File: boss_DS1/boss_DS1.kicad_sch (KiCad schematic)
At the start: 83 parts, among them J2 Jack_6.35, J3 Conn_01x05, J4 Conn_01x05, J5 Conn_01x05, J6 Jack_6.35, J7 Conn_01x01_Socket, J8 Conn_01x01_Socket, J9 Barrel_Jack_Switch, P1 boss_DS1_front_panel, Q1 MMBT5551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

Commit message: Updated front.
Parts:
- added P2: bottom_panel, pedale:bottom_plate, symbol pedale:boss_DS1_front_panel
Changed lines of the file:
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@@
+	)
+	(symbol
+		(lib_id "pedale:boss_DS1_front_panel")
+		(at 242.57 161.29 0)
+		(unit 1)
+		(exclude_from_sim yes)
+		(in_bom no)
+		(on_board yes)
+		(dnp yes)
+		(fields_autoplaced yes)
+		(property "Reference" "P2"
+			(at 245.11 160.0199 0)
+			(effects
+				(font
+					(size 1.27 1.27)
+				)
+				(justify left)
+			)
+		)
+		(property "Value" "bottom_panel"
+			(at 245.11 162.5599 0)
+			(effects
+				(font
+					(size 1.27 1.27)
+				)
+				(justify left)
+			)
+		)
+		(property "Footprint" "pedale:bottom_plate"
+			(at 242.57 161.29 0)
+			(effects
+				(font
+					(size 1.27 1.27)
+				)
+				(hide yes)
+			)
+		)
+		(property "Datasheet" "~"
+			(at 242.57 161.29 0)
+			(effects
+				(font
+					(size 1.27 1.27)
+				)
+				(hide yes)
+			)
+		)
+		(property "Description" "Potentiometer"
+			(at 242.57 161.29 0)
+			(effects
+				(font
+					(size 1.27 1.27)
+				)
+				(hide yes)
+			)
+		)
+		(instances
+			(project "boss_DS1"
+				(path "/e0801131-6974-42d8-8070-4ed960891aa7"
+					(reference "P2")
+					(unit 1)
+				)
+			)
+		)
 	)
 	(symbol

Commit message: Updated libs.
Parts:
- SW1: footprint pedale:foot_switch_tht_and_floating -> pedale:foot_switch_tht_no_pad
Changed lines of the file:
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@@
 			)
 		)
-		(property "Footprint" "pedale:foot_switch_tht_and_floating"
+		(property "Footprint" "pedale:foot_switch_tht_no_pad"
 			(at 168.91 106.68 0)
 			(effects
@@
 			)
 		)
-		(property "Footprint" "pedale:foot_switch_tht_and_floating"
+		(property "Footprint" "pedale:foot_switch_tht_no_pad"
 			(at 168.91 121.92 0)
 			(effects

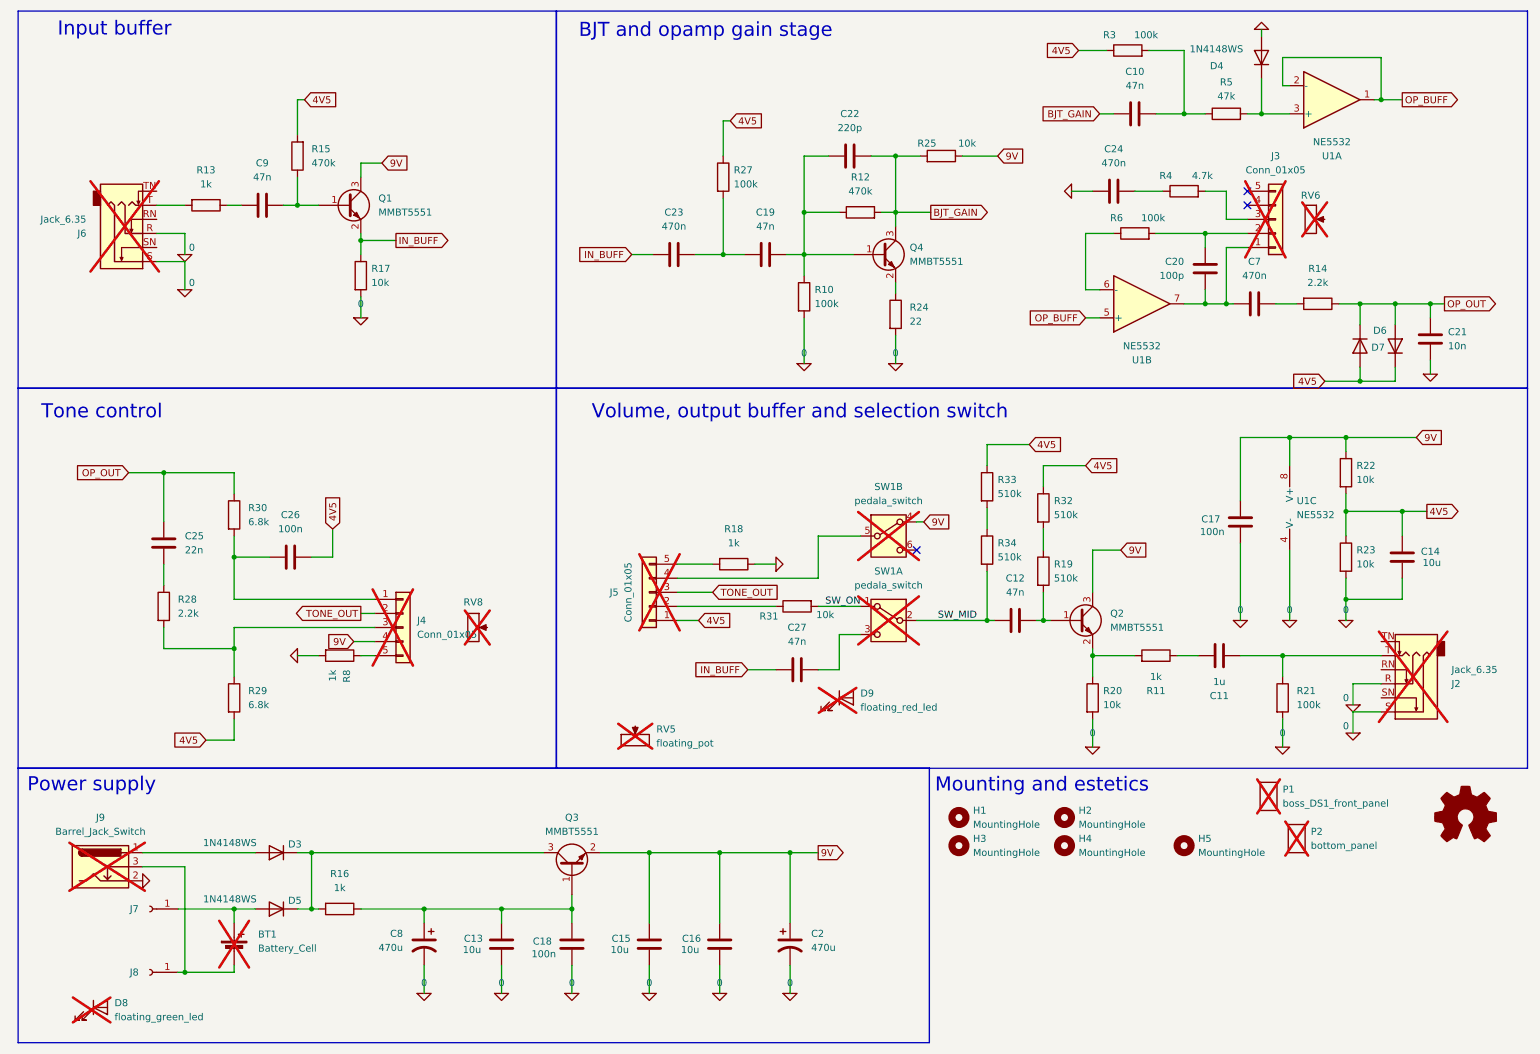
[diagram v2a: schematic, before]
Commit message: Potentiometers checked.
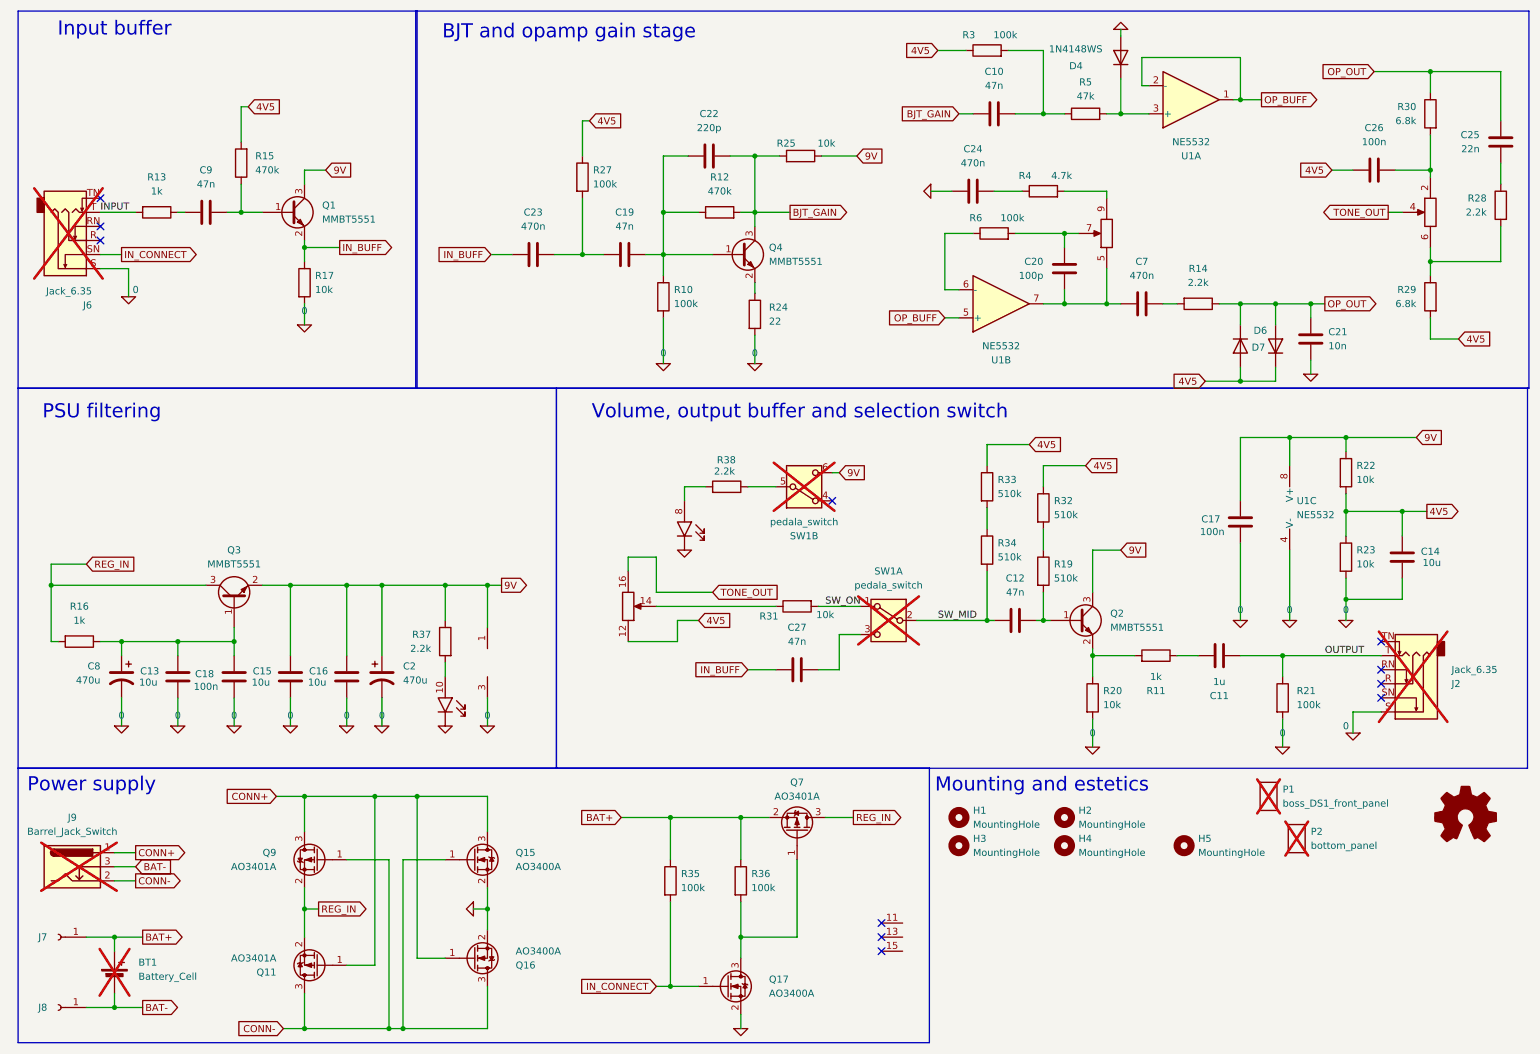
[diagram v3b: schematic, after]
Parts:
- removed D3, D5: 1N4148WS, Diode_SMD:D_SOD-323, symbol Diode:1N4148WS
- removed D8: floating_green_led, pedale:floating_green_led, symbol pedale:floating_green_led
- removed D9: floating_red_led, pedale:floating_red_led, symbol pedale:floating_red_led
- removed J3, J4, J5: Conn_01x05, Connector_JST:JST_EH_B5B-EH-A_1x05_P2.50mm_Vertical, symbol Connector_Generic:Conn_01x05
- removed R18, R8: 1k, Resistor_SMD:R_0603_1608Metric_Pad0.98x0.95mm_HandSolder, symbol Device:R
- removed RV5, RV6, RV8: floating_pot, pedale:floating_pot, symbol pedale:floating_pot
- added J1: top_panel_connector, Connector_IDC:IDC-Header_2x08_P2.54mm_Vertical, symbol pedale:top_panel_connector
- added Q11, Q7, Q9: AO3401A, Package_TO_SOT_SMD:SOT-23, symbol Transistor_FET:AO3401A
- added Q15, Q16, Q17: AO3400A, Package_TO_SOT_SMD:SOT-23, symbol Transistor_FET:AO3400A
- added R35, R36: 100k, Resistor_SMD:R_0603_1608Metric_Pad0.98x0.95mm_HandSolder, symbol Device:R
- added R37, R38: 2.2k, Resistor_SMD:R_0603_1608Metric_Pad0.98x0.95mm_HandSolder, symbol Device:R
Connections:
- net 0: now also J1.3 (GND), Q15.2 (S), Q16.2 (S), Q17.2 (S); no longer J2.R, J6.R, J9.2
- net 4V5: now also J1.12 (Pin_12)
- net 9V: now also SW1.6 (C), J1.1 (VCC), R37.1; no longer SW1.4 (A)
- net TONE_OUT: now also J1.16 (Pin_16), J1.4 (Pin_4)
- net REG_IN: now reaches Q3.3 (C), R16.2
- net REG_IN: now also Q11.2 (S), Q7.3 (D), Q9.2 (S)
- net at C26.1, R30.2: now also J1.2 (Pin_2)
- net at R28.2, R29.1: now also J1.6 (Pin_6)
- net BAT+: now reaches BT1.1 (+), J7.1 (Pin_1)
- net BAT+: now also Q7.2 (S), R35.1, R36.1
- net CONN+: now reaches J9.1
- net CONN+: now also Q11.1 (G), Q15.3 (D), Q16.1 (G), Q9.3 (D)
- net BAT-: now reaches BT1.2 (-), J8.1 (Pin_1), J9.3
- net at SW1.5 (B): now also R38.1
- net OUTPUT: now reaches C11.2, J2.T, R21.1
- net at R31.1: now also J1.14 (Pin_14)
- net at R4.2: now also J1.9 (Pin_9)
- net at C20.1, C7.1, U1.7: now also J1.5 (Pin_5)
- net at C20.2, R6.2: now also J1.7 (Pin_7)
- net IN_CONNECT: now reaches J6.SN
- net IN_CONNECT: now also Q17.1 (G), R35.2
- net INPUT: now reaches J6.T, R13.2
- new net: J1.10 (Pin_10), R37.2
- new net: Q17.3 (D), Q7.1 (G), R36.2
- new net: J1.8 (Pin_8), R38.2
- new net CONN-: J9.2, Q11.3 (D), Q15.1 (G), Q16.3 (D), Q9.1 (G)
- no-connect marks 3 -> 11
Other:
- note added: "PSU filtering"
- note removed: "Tone control"
- moved on the sheet: BT1, C10, C13, C15, C16, C18, C19, C2, C20, C21, C22, C23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

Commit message: Pots again, done.
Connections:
- net 4V5: now also J1.16 (Pin_16); no longer J1.12 (Pin_12)
- net TONE_OUT: now also J1.12 (Pin_12); no longer J1.16 (Pin_16)
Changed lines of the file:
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@@
 		(lib_id "pedale:top_panel_connector")
 		(at 121.92 119.38 0)
-		(mirror x)
 		(unit 3)
 		(exclude_from_sim no)
@@
 		(dnp no)
 		(property "Reference" "J1"
-			(at 122.936 127.762 0)
+			(at 122.936 110.998 0)
 			(effects
 				(font
@@
 		)
 		(property "Value" "top_panel_connector"
-			(at 124.46 114.3 0)
+			(at 124.46 124.46 0)
 			(effects
 				(font
@@
 		)
 		(property "Description" ""
-			(at 107.95 79.756 0)
+			(at 107.95 159.004 0)
 			(effects
 				(font

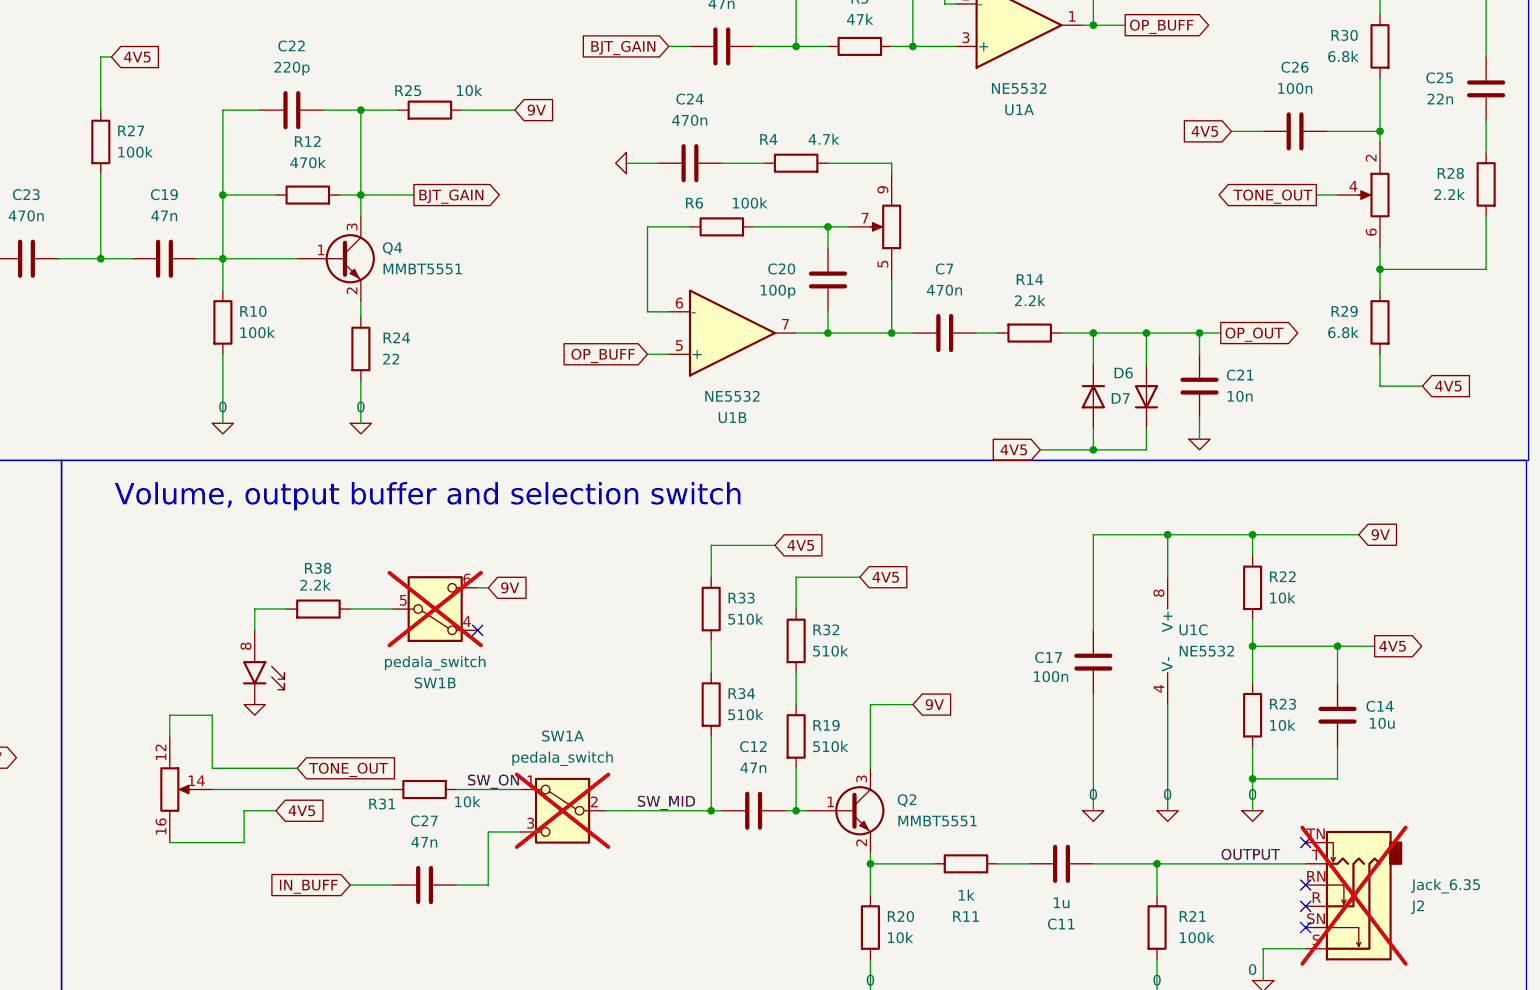
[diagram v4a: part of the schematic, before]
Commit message: Top plate routiran, valja proveriti pot-ove opet.
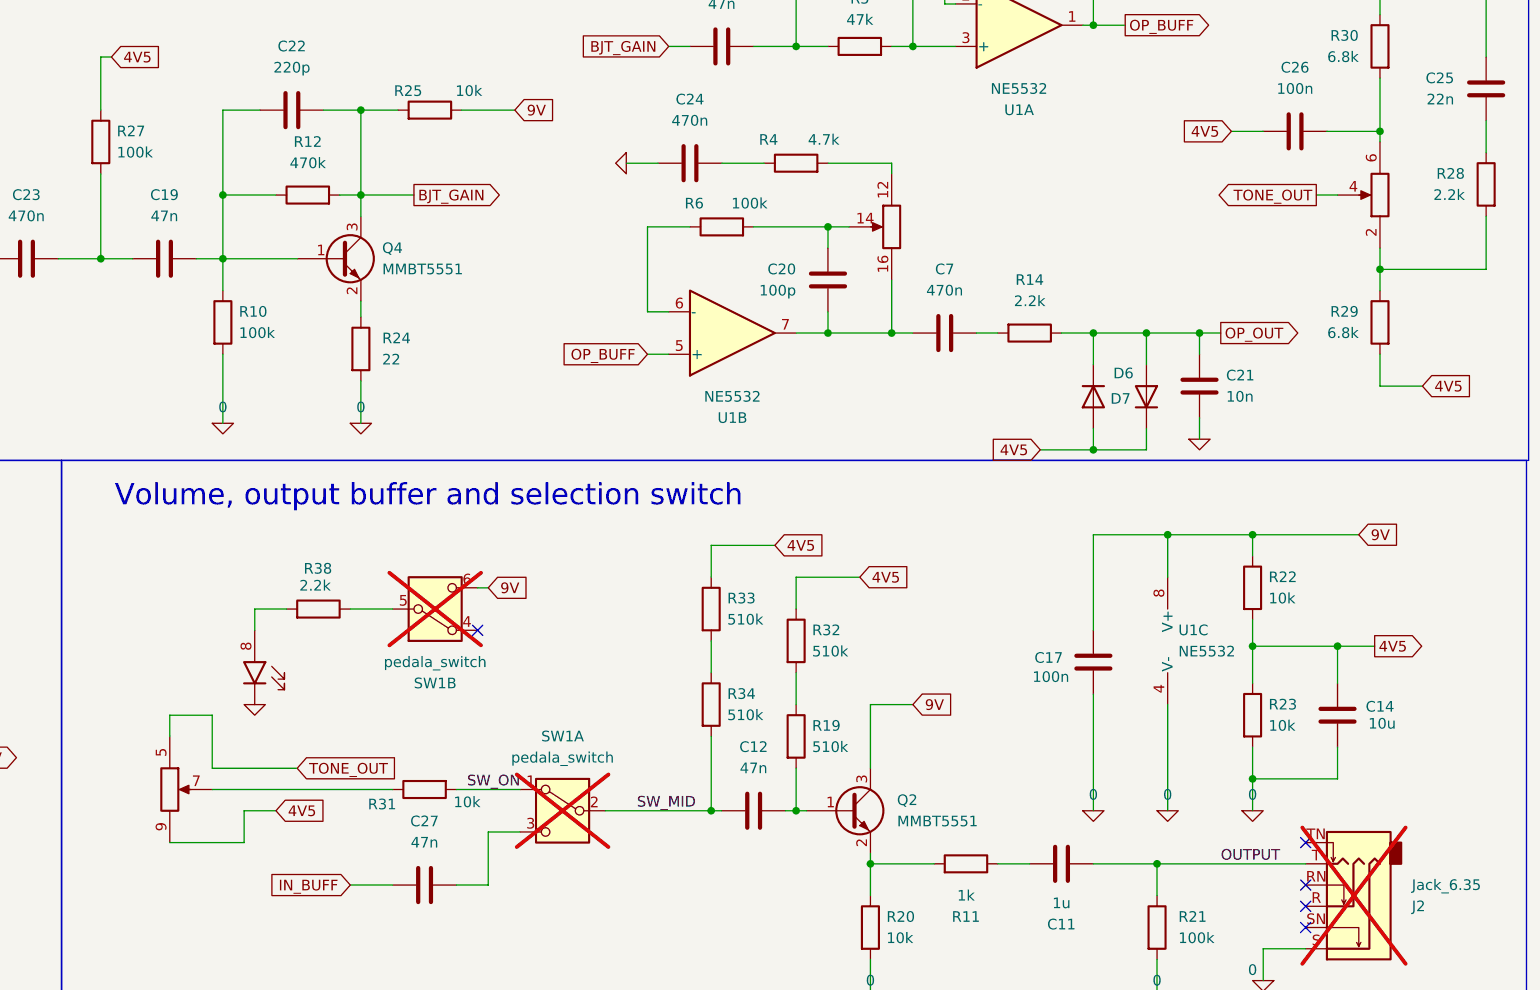
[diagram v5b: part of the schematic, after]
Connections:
- net 4V5: now also J1.9 (Pin_9); no longer J1.16 (Pin_16)
- net TONE_OUT: now also J1.5 (Pin_5); no longer J1.12 (Pin_12)
- net at C26.1, R30.2: now also J1.6 (Pin_6); no longer J1.2 (Pin_2)
- net at R31.1: now also J1.7 (Pin_7); no longer J1.14 (Pin_14)
- net at R28.2, R29.1: now also J1.2 (Pin_2); no longer J1.6 (Pin_6)
- net at C20.1, C7.1, U1.7: now also J1.16 (Pin_16); no longer J1.5 (Pin_5)
- net at C20.2, R6.2: now also J1.14 (Pin_14); no longer J1.7 (Pin_7)
- net at R4.2: now also J1.12 (Pin_12); no longer J1.9 (Pin_9)
